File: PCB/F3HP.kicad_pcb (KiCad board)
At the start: 2 copper layers, 96.9 x 107.7 mm, 108 parts, among them J1 L_In, J2 R_In, J3 AC_In, J4 Switch, J5 HPOut, K1 C93402, Q1 BC850C, Q10 BC860C, Q2 BC860C, Q3 BCP56, Q4 BC850C, Q5 BC860C, Q6 BCP56, Q7 BC850C, Q8 AO3400A, Q9 BC860C, U1 LT1965

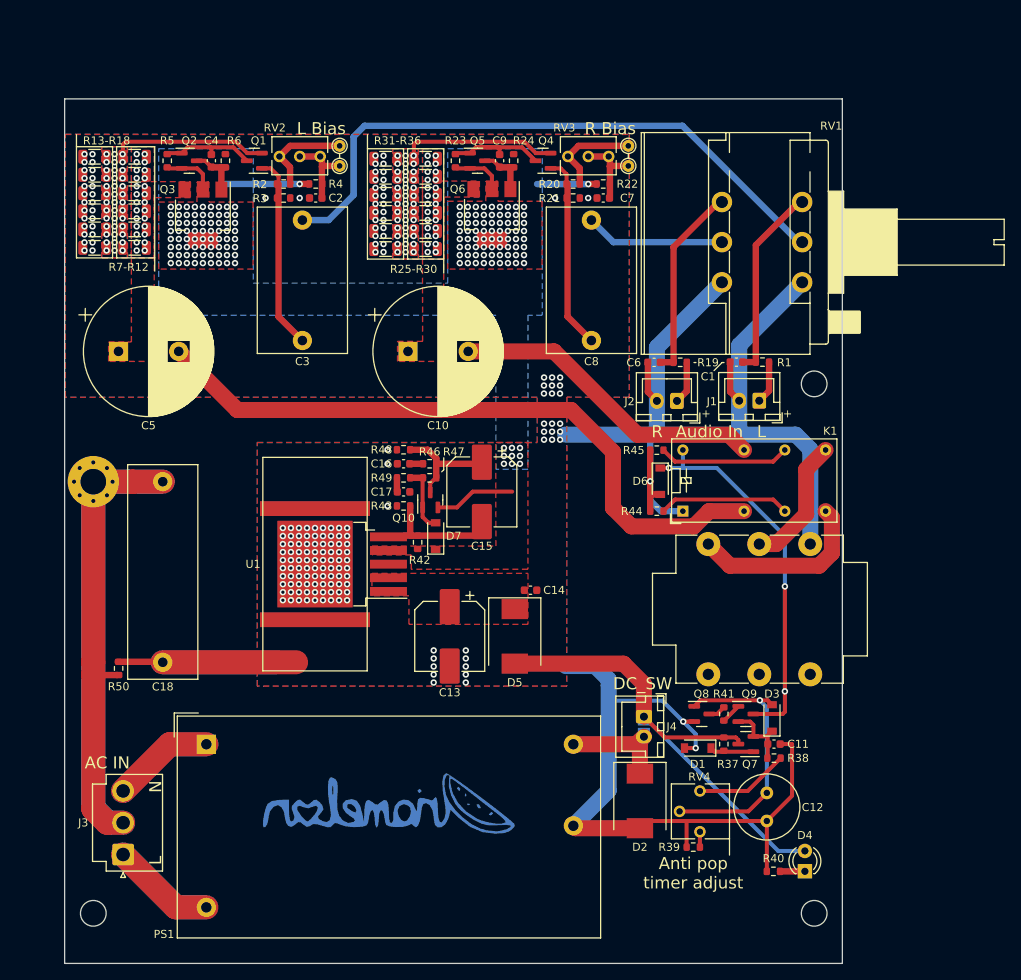
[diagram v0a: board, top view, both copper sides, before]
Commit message: Better layout, better heatsinking
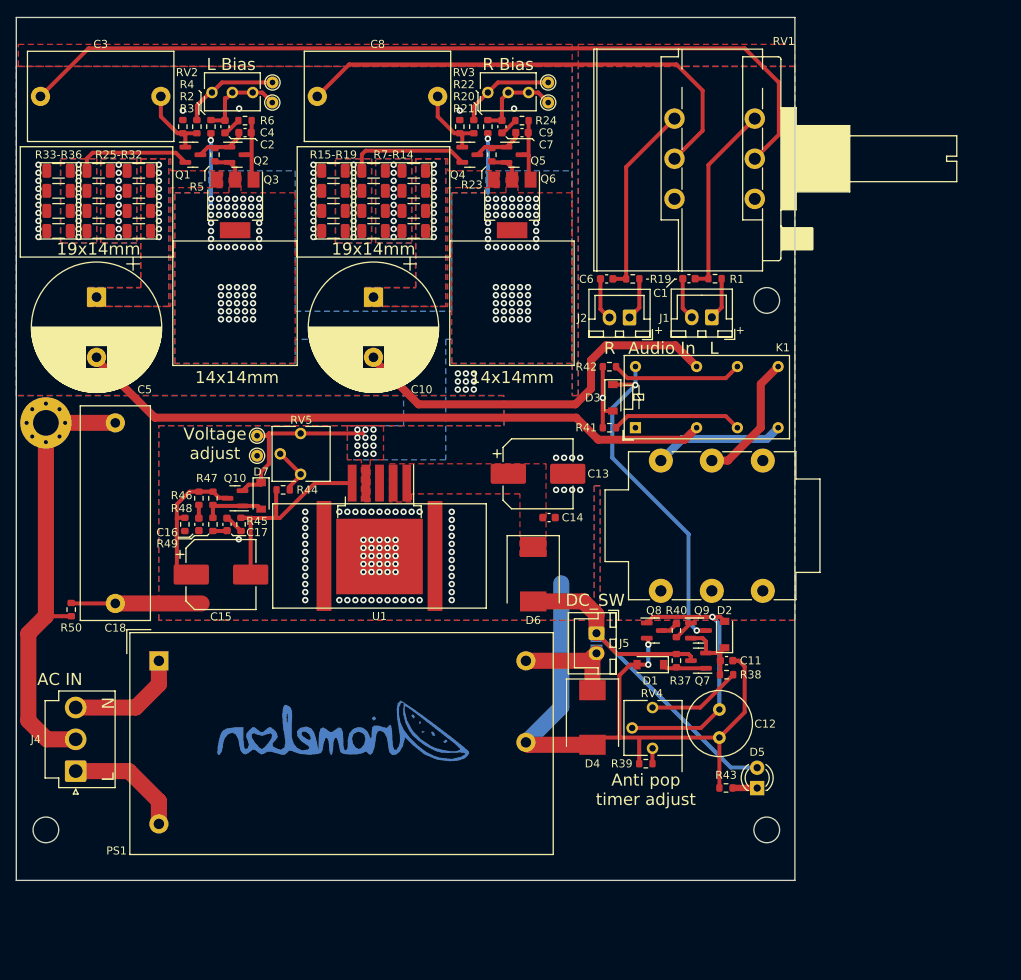
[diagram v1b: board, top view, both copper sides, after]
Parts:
- removed the R34 at (96.0, 46.5)
- removed the R35 at (96.0, 44.2)
- added R31: 133, Resistor_SMD:R_1206_3216Metric, F.Cu at (99.5, 51.0)
- added R32: 133, Resistor_SMD:R_1206_3216Metric, F.Cu at (94.5, 51.0)
- added RV5: 500, Potentiometer_THT:Potentiometer_Vishay_T73YP_Vertical, F.Cu at (85.4, 76.2)
- added TP5: TestPoint, TestPoint:TestPoint_THTPad_D1.5mm_Drill0.7mm, F.Cu at (80.0, 79.0)
- added TP6: TestPoint, TestPoint:TestPoint_THTPad_D1.5mm_Drill0.7mm, F.Cu at (80.0, 76.5)
- R10, R11, R12, R25, R30, R7, R8, R9: value 330 -> 133
- R13, R14: value 220 -> 133
- R15, R16, R17, R18, R36: value 220 -> 93.1
- R26: renamed from R28; value 330 -> 133
- R27: renamed from R26; value 330 -> 133
- R28: renamed from R29; value 330 -> 133
- R29: renamed from R27; value 330 -> 133
- R33: renamed from R31; value 220 -> 93.1
- R34: renamed from R32; value 220 -> 93.1
- R35: renamed from R33; value 220 -> 93.1
- R44: renamed from R42; value 2.4k -> 2.2k
- moved C8 37.5 mm to (87.5, 34.2), turned to 0 degrees
- moved C3 36.1 mm to (53.0, 34.2), turned to 0 degrees
- moved C15 34.1 mm to (75.5, 93.8), turned to 0 degrees
- moved R46 29.1 mm to (72.8, 84.3), turned to 90 degrees
- moved R48 28.8 mm to (71.0, 87.5), turned to 90 degrees
- moved R47 27.1 mm to (74.5, 84.3), turned to -90 degrees
- moved C16 26.6 mm to (72.8, 87.5), turned to -90 degrees
- moved R49 24.4 mm to (74.5, 87.5), turned to 90 degrees
- moved Q10 24.3 mm to (77.2, 84.3), turned to 180 degrees
- moved C13 23.0 mm to (115.0, 81.2), turned to 0 degrees
- moved C17 22.4 mm to (76.2, 87.5), turned to 90 degrees
- moved D7 22.3 mm to (80.5, 84.0), turned to -90 degrees
- moved R45 20.4 mm to (78.0, 87.5), turned to 90 degrees
- moved R44 18.0 mm to (83.2, 83.2), turned to 0 degrees
- moved R21 16.7 mm to (105.2, 38.0), turned to 90 degrees
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- renumbered D3 to D2, D6 to D3, D2 to D4, D4 to D5, D5 to D6, J5 to J3, J3 to J4, J4 to J5, R41 to R40, R44 to R41, R45 to R42, R40 to R43, R43 to R45
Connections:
- C10 pad 1: Net-(Q6-Pad3) -> Net-(C10-Pad1)
- Q1 pad 2: Net-(R13-Pad1) -> Net-(Q1-Pad2)
- Q6 pad 3: Net-(Q6-Pad3) -> Net-(C10-Pad1)
- R10 pad 1: Net-(C5-Pad1) -> Net-(R10-Pad1)
- R10 pad 2: Net-(R13-Pad1) -> Net-(Q1-Pad2)
- R11 pad 2: Net-(R13-Pad1) -> Net-(R10-Pad1)
- R12 pad 1: Net-(C5-Pad1) -> Net-(R10-Pad1)
- R12 pad 2: Net-(R13-Pad1) -> Net-(Q1-Pad2)
- R13 pad 1: Net-(R13-Pad1) -> Net-(C5-Pad1)
- R13 pad 2: GND -> Net-(R10-Pad1)
- R14 pad 1: Net-(R13-Pad1) -> Net-(R10-Pad1)
- R14 pad 2: GND -> Net-(Q1-Pad2)
- R15 pad 1: Net-(R13-Pad1) -> Net-(Q1-Pad2)
- R16 pad 1: Net-(R13-Pad1) -> Net-(Q1-Pad2)
- R17 pad 1: Net-(R13-Pad1) -> Net-(Q1-Pad2)
- R18 pad 1: Net-(R13-Pad1) -> Net-(Q1-Pad2)
- R25 pad 1: Net-(Q6-Pad3) -> Net-(C10-Pad1)
- R25 pad 2: Net-(Q4-Pad2) -> Net-(R25-Pad2)
- R26 pad 1: Net-(Q6-Pad3) -> Net-(R25-Pad2)
- R27 pad 1: Net-(Q6-Pad3) -> Net-(C10-Pad1)
- R27 pad 2: Net-(Q4-Pad2) -> Net-(R25-Pad2)
- R28 pad 1: Net-(Q6-Pad3) -> Net-(R25-Pad2)
- R29 pad 1: Net-(Q6-Pad3) -> Net-(C10-Pad1)
- R29 pad 2: Net-(Q4-Pad2) -> Net-(R25-Pad2)
- R30 pad 1: Net-(Q6-Pad3) -> Net-(R25-Pad2)
- R44 pad 2: +12V -> Net-(R44-Pad2)
- R7 pad 2: Net-(R13-Pad1) -> Net-(R10-Pad1)
- R8 pad 1: Net-(C5-Pad1) -> Net-(R10-Pad1)
- R8 pad 2: Net-(R13-Pad1) -> Net-(Q1-Pad2)
- R9 pad 2: Net-(R13-Pad1) -> Net-(R10-Pad1)
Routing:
- net GND: track 242.9 -> 123.8 mm, vias 180 -> 116
- net GNDPWR: track 110.8 -> 56.7 mm
- net Net-(C8-Pad1): track 17.4 -> 60.9 mm
- net Net-(C3-Pad1): track 77.1 -> 107.0 mm
- net Net-(R13-Pad1): track 19.3 -> 0.00 mm, vias 39 -> 0
- net Net-(D3-Pad1): track 60.4 -> 42.4 mm, vias 3 -> 2
- net Net-(C15-Pad2): track 12.8 -> 27.5 mm
- net Net-(Q1-Pad2): track 0.00 -> 14.6 mm, vias 0 -> 10
- net Net-(C8-Pad2): track 24.2 -> 9.73 mm
- net Net-(C3-Pad2): track 24.2 -> 9.72 mm
- net Net-(J4-Pad1): track 26.2 -> 14.8 mm
- net Net-(J4-Pad3): track 25.6 -> 14.5 mm
- net +15V: track 62.0 -> 51.3 mm
- net R_Out: track 39.4 -> 49.1 mm
- net Net-(C9-Pad2): track 14.7 -> 6.30 mm
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- added copper zone on B.Cu, net Net-(C10-Pad1)
- added copper zone on F.Cu, net Net-(C10-Pad1)
- added copper zone on B.Cu, net Net-(Q1-Pad2)
- added copper zone on F.Cu, net Net-(Q1-Pad2)
- added copper zone on B.Cu, net Net-(R10-Pad1)
- added copper zone on F.Cu, net Net-(R10-Pad1)
- added copper zone on B.Cu, net Net-(R25-Pad2)
- added copper zone on F.Cu, net Net-(R25-Pad2)
- removed copper zone on B.Cu, net Net-(Q6-Pad3)
- removed copper zone on F.Cu, net Net-(Q6-Pad3)
- removed copper zone on B.Cu, net Net-(R13-Pad1)
- removed copper zone on F.Cu, net Net-(R13-Pad1)
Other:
- board size 96.9 x 107.7 mm -> 97 x 107.5 mm
- board text added: "14x14mm"
- board text added: "19x14mm"
- board text added: "R15-R19"
- board text added: "R25-R32"
- board text added: "R33-R36"
- board text added: "R7-R14"
- board text added: "Voltage adjust"
- board text removed: "R11"
- board text removed: "R13-R18"
- board text removed: "R25-R30"
- board text removed: "R31-R36"
- board text removed: "R6"
- board text removed: "R7-R12"

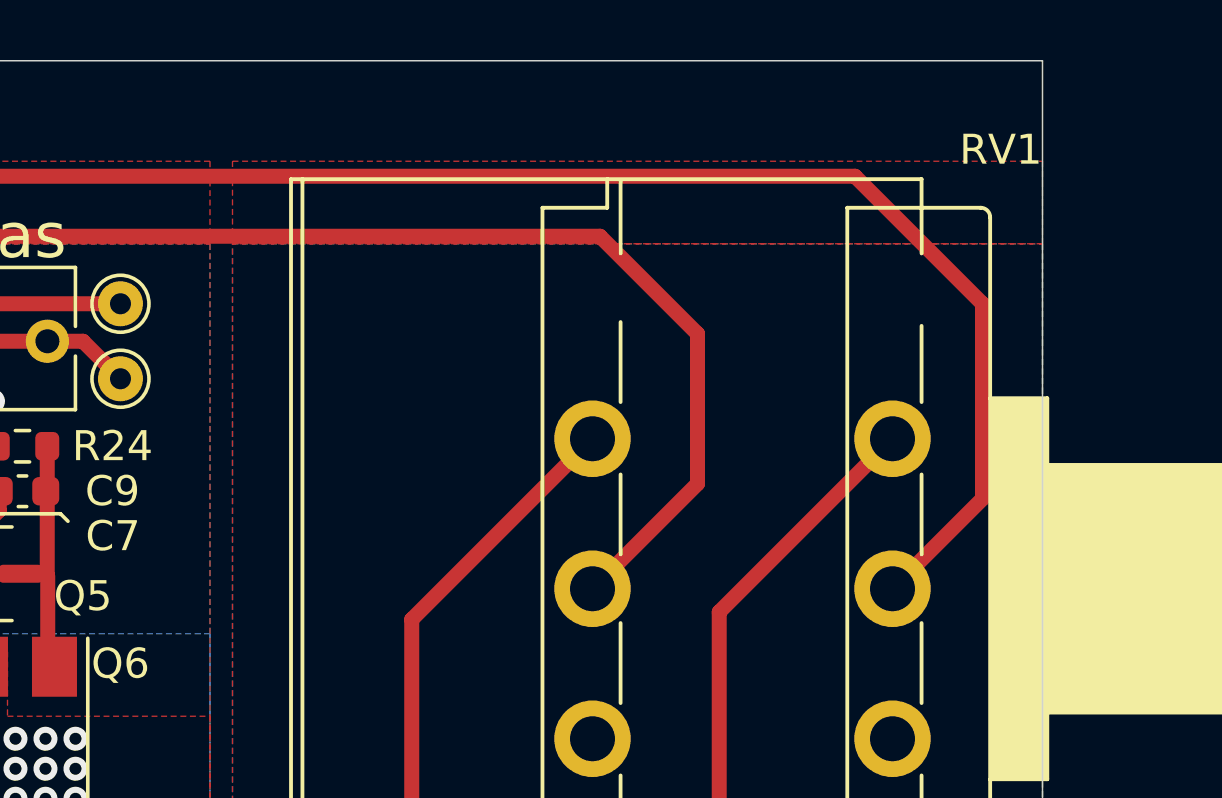
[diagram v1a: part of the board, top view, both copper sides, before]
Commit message: Updated component values and BOM
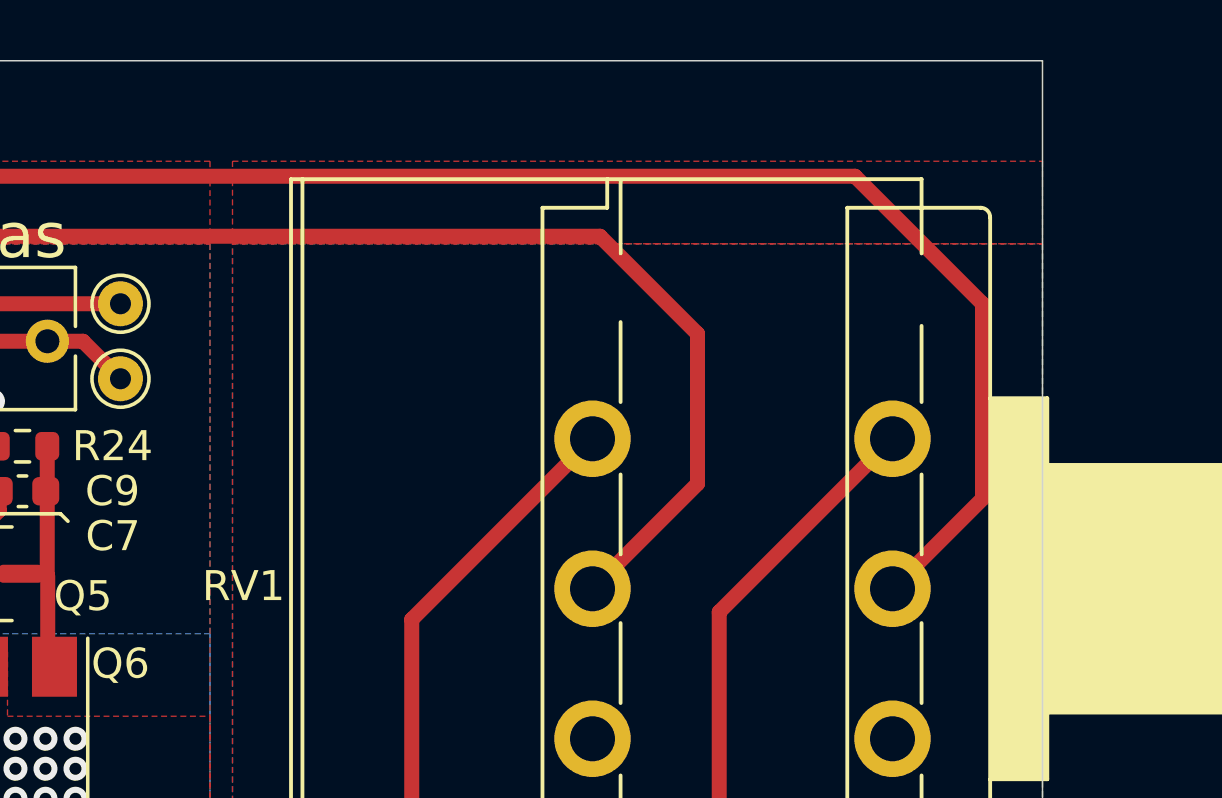
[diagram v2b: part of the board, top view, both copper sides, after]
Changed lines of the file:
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@@
     (property "Sheetname" "")
     (attr through_hole)
-    (fp_text reference "RV1" (at -14.04584 -9.992) (layer "F.SilkS")
+    (fp_text reference "RV1" (at 0.5 15.25) (layer "F.SilkS")
       (effects (font (size 1 1) (thickness 0.15)) (justify right bottom))
     )
@@
     (fp_line (start 3.56 -5.96) (end 3.56 0.88) (layer "F.SilkS") (width 0.12))
     (fp_line (start 0.65 -5.96) (end 3.56 -5.96) (layer "F.SilkS") (width 0.12))
-    (fp_line (start -3.68 -5.96) (end -0.65 -5.96) (layer "F.SilkS") (width 0.12))
     (fp_line (start 0.65 0.88) (end 3.56 0.88) (layer "F.SilkS") (width 0.12))
     (fp_line (start -3.68 -5.96) (end -3.68 0.88) (layer "F.SilkS") (width 0.12))
     (fp_line (start -3.68 0.88) (end -0.65 0.88) (layer "F.SilkS") (width 0.12))
+    (fp_line (start -3.68 -5.96) (end -0.65 -5.96) (layer "F.SilkS") (width 0.12))
     (fp_line (start -3.85 1.05) (end 3.7 1.05) (layer "F.CrtYd") (width 0.05))
     (fp_line (start 3.7 -6.1) (end -3.85 -6.1) (layer "F.CrtYd") (width 0.05))

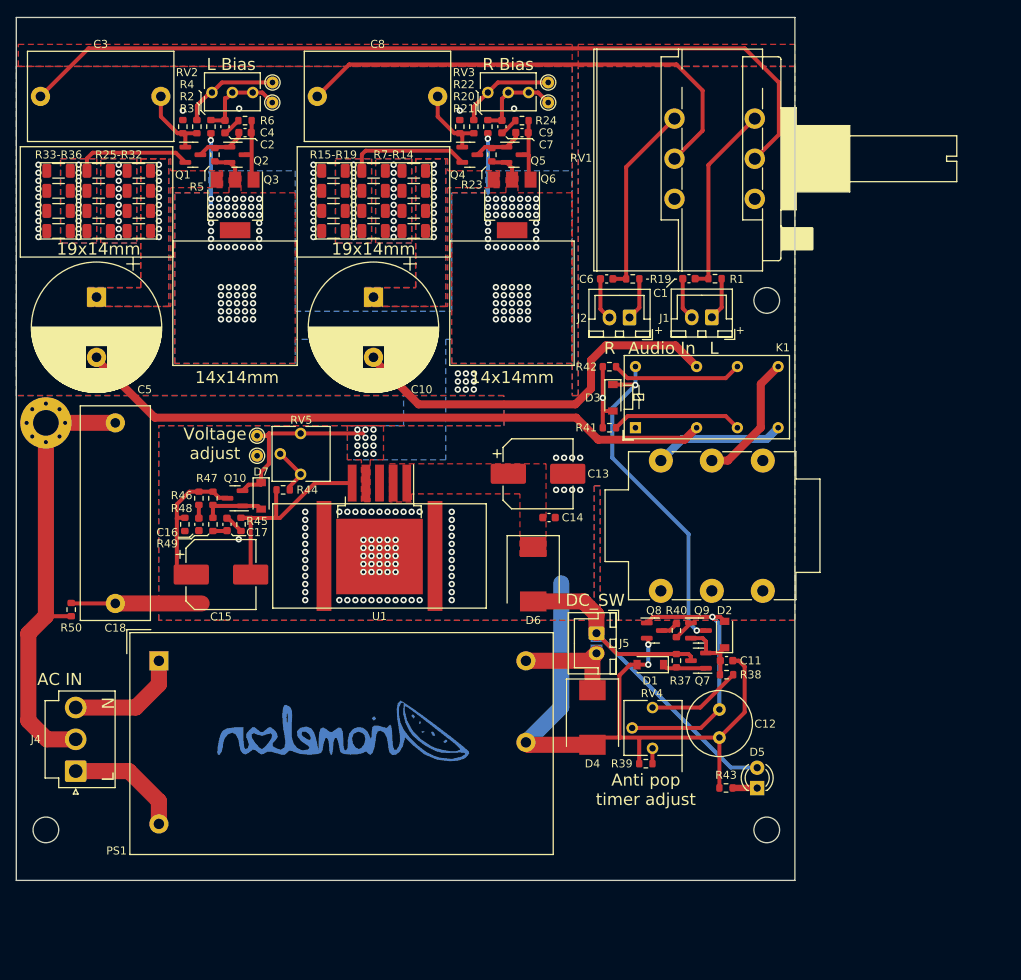
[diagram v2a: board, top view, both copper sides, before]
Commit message: Swapped to TPS7A4701 LDO, better performance and less complicated PCB required
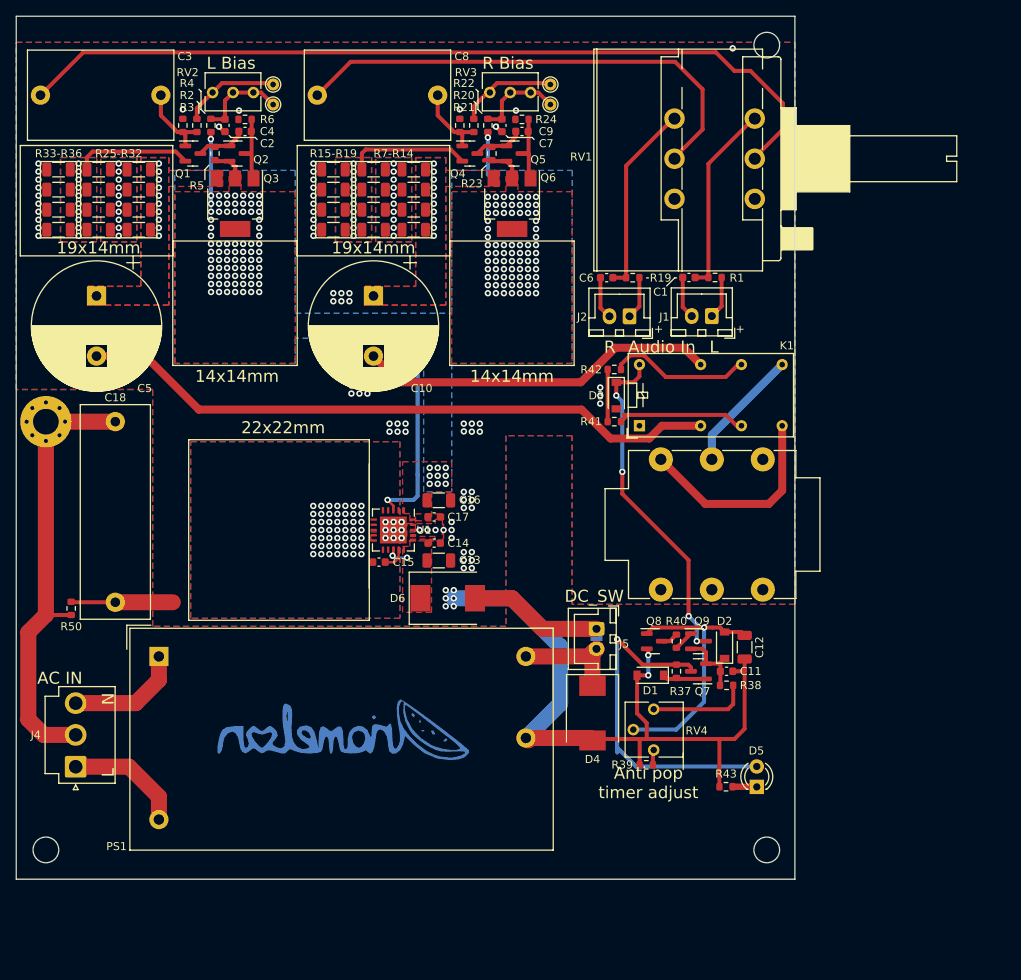
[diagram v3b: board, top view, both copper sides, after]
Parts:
- removed D7: D, Diode_SMD:D_SOD-123
- removed HS1: Heatsink, Heatsink:Heatsink_AAVID_573300D00010G_TO-263
- removed Q10: BC860C, Package_TO_SOT_SMD:SOT-23
- removed R44: 2.2k, Resistor_SMD:R_0603_1608Metric
- removed R45: 270, Resistor_SMD:R_0603_1608Metric
- removed R46: 33, Resistor_SMD:R_0603_1608Metric
- removed R47: 180k, Resistor_SMD:R_0603_1608Metric
- removed R48: 1.8k, Resistor_SMD:R_0603_1608Metric
- removed R49: 22, Resistor_SMD:R_0603_1608Metric
- removed RV5: 500, Potentiometer_THT:Potentiometer_Vishay_T73YP_Vertical
- removed TP5, TP6: TestPoint, TestPoint:TestPoint_THTPad_D1.5mm_Drill0.7mm
- C12: footprint Capacitor_THT:C_Radial_D8.0mm_H11.5mm_P3.50mm -> Capacitor_SMD:C_1206_3216Metric
- C13: value 470u -> 47u; footprint Capacitor_SMD:CP_Elec_8x10.5 -> Capacitor_SMD:C_1206_3216Metric
- C15: value 470u -> 1u; footprint Capacitor_SMD:CP_Elec_8x10.5 -> Capacitor_SMD:C_0603_1608Metric
- C16: value 10n -> 47u; footprint Capacitor_SMD:C_0603_1608Metric -> Capacitor_SMD:C_1206_3216Metric
- Q3, Q6: value BCP56 -> BCP56TA
- R1, R19: value 2k2 -> 2.2k
- R22, R4: value 47k -> 39k
- R23, R5: value 1k -> 820
- R24, R6: value 1k -> 1.2k
- RV2, RV3: value 50k -> 5k
- U1: value LT1965 -> TPS7A4701RGWR; footprint Package_TO_SOT_SMD:TO-263-5_TabPin3 -> Package_DFN_QFN:QFN-20-1EP_5x5mm_P0.65mm_EP3.35x3.35mm
- moved H1 31.8 mm to (143.5, 27.9)
- moved C16 30.0 mm to (102.6, 84.5), turned to 0 degrees
- moved C17 25.8 mm to (102.1, 86.6), turned to 0 degrees
- moved C15 19.7 mm to (95.2, 92.2), turned to 180 degrees
- moved C13 16.4 mm to (102.6, 92.0)
- moved C14 14.7 mm to (102.1, 89.9)
- moved C12 11.7 mm to (140.7, 102.8), turned to -90 degrees
- moved D6 11.1 mm to (103.8, 96.8), turned to 0 degrees
- moved H2 2.49 mm to (143.5, 128.1)
- moved H3 2.49 mm to (53.7, 128.1)
- moved U1 1.73 mm to (97.0, 88.2)
- moved C11 1.33 mm to (138.5, 105.8)
- moved D1 1.33 mm to (129.0, 106.3)
- moved D2 1.33 mm to (138.2, 102.6)
- moved Q7 1.33 mm to (135.0, 105.8)
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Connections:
- C12 pad 1: GND -> Net-(D2-Pad2)
- C12 pad 2: Net-(C12-Pad2) -> GND
- C15 pad 2: Net-(C15-Pad2) -> GND
- C16 pad 1: Net-(C16-Pad1) -> +12V
- C17 pad 1: Net-(C17-Pad1) -> +12V
- D2 pad 2: Net-(C12-Pad2) -> Net-(D2-Pad2)
- Q8 pad 1: Net-(C12-Pad2) -> Net-(D2-Pad2)
- RV4 pad 2: Net-(C12-Pad2) -> Net-(D2-Pad2)
- U1 pad 1: Net-(C13-Pad1) -> +12V
- U1 pad 2: Net-(C13-Pad1) -> GND
- U1 pad 3: GND -> +12V
- U1 pad 4: +12V -> unconnected-(U1-Pad4)
- U1 pad 5: Net-(C15-Pad2) -> GND
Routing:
- net Net-(C12-Pad2): track 33.9 -> 0.00 mm, vias 1 -> 0
- net Net-(D2-Pad2): track 0.00 -> 32.4 mm, vias 0 -> 1
- net Net-(C15-Pad2): track 27.5 -> 0.00 mm
- net Net-(C15-Pad1): track 16.3 -> 3.19 mm
- net Net-(J3-PadT): track 16.3 -> 26.2 mm
- net +15V: track 51.3 -> 60.4 mm, vias 0 -> 1
- net Net-(D7-Pad2): track 7.64 -> 0.00 mm
- net Net-(R44-Pad2): track 6.26 -> 0.00 mm
- net R_Out: track 49.1 -> 44.8 mm
- net Net-(C13-Pad1): track 0.00 -> 3.19 mm, vias 0 -> 2
- net +12V: track 48.5 -> 51.3 mm, vias 132 -> 164
- net Net-(C17-Pad1): track 1.70 -> 0.00 mm
- net Net-(C16-Pad1): track 1.65 -> 0.00 mm
- net Net-(C3-Pad1): track 107.0 -> 105.5 mm
- net GND: track 123.8 -> 122.7 mm, vias 116 -> 142
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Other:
- board text added: "22x22mm"
- board text removed: "Voltage adjust"

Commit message: Errors fixed
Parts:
- U1: value TPS7A4701RGWR -> TPS7A4701
- moved H1 32.1 mm to (143.5, 60.0)
- moved C15 0.59 mm to (95.5, 92.8)
- moved C12 0.35 mm to (140.8, 102.5)
- moved D4 0.25 mm to (121.8, 111.3)
- moved JP1 0.21 mm to (122.3, 102.0)
- moved J5 0.19 mm to (122.3, 100.8)
- moved C11 0.10 mm to (138.5, 105.8)
- moved D1 0.10 mm to (129.0, 106.2)
- moved D2 0.10 mm to (138.2, 102.5)
- moved Q7 0.10 mm to (135.0, 105.8)
- moved Q8 0.10 mm to (129.5, 102.0)
- moved Q9 0.10 mm to (135.0, 102.0)
- moved R37 0.10 mm to (132.2, 105.8)
- moved R38 0.10 mm to (138.5, 107.5)
- moved R40 0.10 mm to (132.2, 102.0)
- renumbered R50 to R44
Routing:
- net +15V: track 60.4 -> 62.9 mm
- net GND: track 122.7 -> 120.4 mm, vias 142 -> 143
- net +12V: track 51.3 -> 50.0 mm
- net Net-(D4-Pad1): track 14.0 -> 13.3 mm
- net Net-(C12-Pad1): track 32.4 -> 31.8 mm
- net Net-(K1-Pad6): track 16.0 -> 15.5 mm
